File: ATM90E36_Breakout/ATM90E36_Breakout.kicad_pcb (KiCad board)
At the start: 2 copper layers, 50 x 50 mm, 75 parts, among them IC1 ATM90E36, Q1 FA-128

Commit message: Fix references and SCH/PCB linkage
Signed-off-by: Tisham Dhar <whatnickd@gmail.com>
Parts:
- renumbered CTA to CTA1, CTB to CTB1, CTC to CTC1, CTN to CTN1, DMA to DMA1, UAUB to UAUB1, UCUN to UCUN1
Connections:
- net CF1 renamed /CF1
- net CF2 renamed /CF2
- net CF3 renamed /CF3
- net CF4 renamed /CF4
- net DMA renamed /DMA
- net IA+ renamed /IA+
- net IA- renamed /IA-
- net IAN renamed /IAN
- net IAP renamed /IAP
- net IB+ renamed /IB+
- net IB- renamed /IB-
- net IBN renamed /IBN
- net IBP renamed /IBP
- net IC+ renamed /IC+
- net IC- renamed /IC-
- net ICN renamed /ICN
- net ICP renamed /ICP
- net IN+ renamed /IN+
- net IN- renamed /IN-
- net INN renamed /INN
- net INP renamed /INP
- net IRQ1 renamed /IRQ1
- net IRQ2 renamed /IRQ2
- net MISO renamed /MISO
- net MOSI renamed /MOSI
- net PM0 renamed /PM0
- net PM1 renamed /PM1
- net SCLK renamed /SCLK
- net UA renamed /UA
- net UB renamed /UB
- net UC renamed /UC
- net VAP renamed /VAP
- net VBP renamed /VBP
- net VCP renamed /VCP
- net WARN renamed /WARN
- net ZX0 renamed Net-(IC1-Pad22)
- net ZX1 renamed Net-(IC1-Pad23)
- net ZX2 renamed Net-(IC1-Pad24)
- net ~CS renamed /~CS
- CTA1 pad COM2: (no net) -> Net-(CTA1-PadCOM2)
- CTA1 pad LS: (no net) -> Net-(CTA1-PadLS)
- CTA1 pad R: (no net) -> Net-(CTA1-PadR)
- CTA1 pad RS: (no net) -> Net-(CTA1-PadRS)
- CTB1 pad COM2: (no net) -> Net-(CTB1-PadCOM2)
- CTB1 pad LS: (no net) -> Net-(CTB1-PadLS)
- CTB1 pad R: (no net) -> Net-(CTB1-PadR)
- CTB1 pad RS: (no net) -> Net-(CTB1-PadRS)
- CTC1 pad COM2: (no net) -> Net-(CTC1-PadCOM2)
- CTC1 pad LS: (no net) -> Net-(CTC1-PadLS)
- CTC1 pad R: (no net) -> Net-(CTC1-PadR)
- CTC1 pad RS: (no net) -> Net-(CTC1-PadRS)
- CTN1 pad COM2: (no net) -> Net-(CTN1-PadCOM2)
- CTN1 pad LS: (no net) -> Net-(CTN1-PadLS)
- CTN1 pad R: (no net) -> Net-(CTN1-PadR)
- CTN1 pad RS: (no net) -> Net-(CTN1-PadRS)
- IC1 pad 35: (no net) -> Net-(IC1-Pad35)
- IC1 pad 45: (no net) -> Net-(IC1-Pad45)
- IC1 pad 46: (no net) -> Net-(IC1-Pad46)

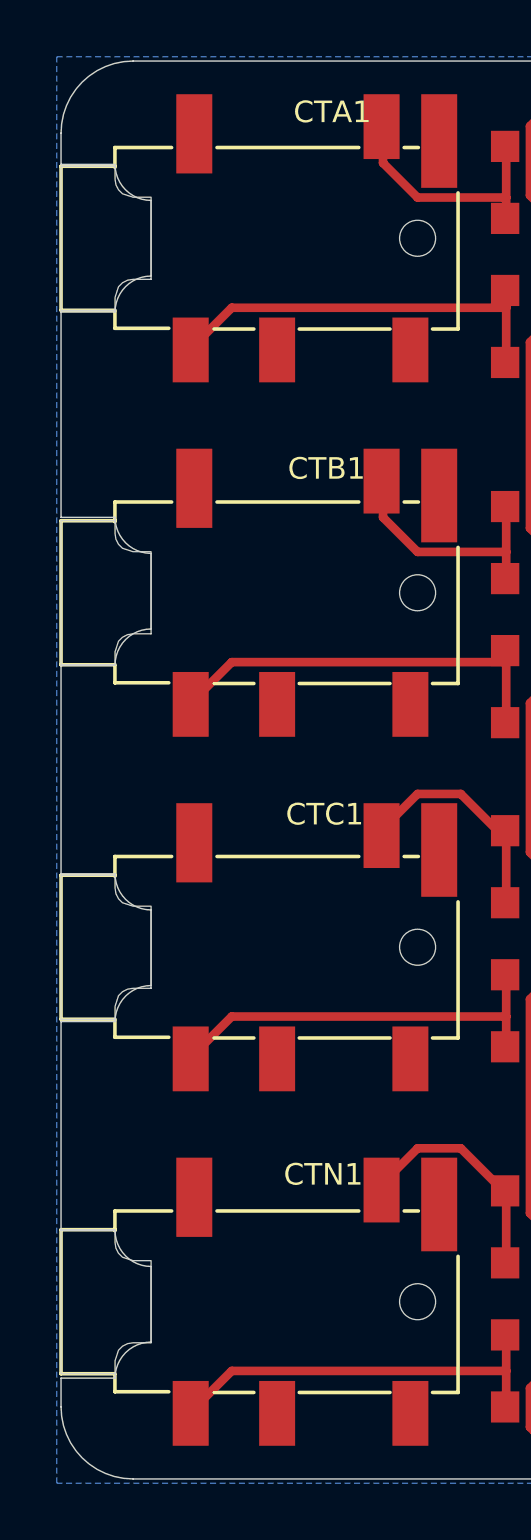
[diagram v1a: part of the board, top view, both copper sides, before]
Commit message: Remove edge cuts from parts to fix board outline
Signed-off-by: Tisham Dhar <whatnickd@gmail.com>
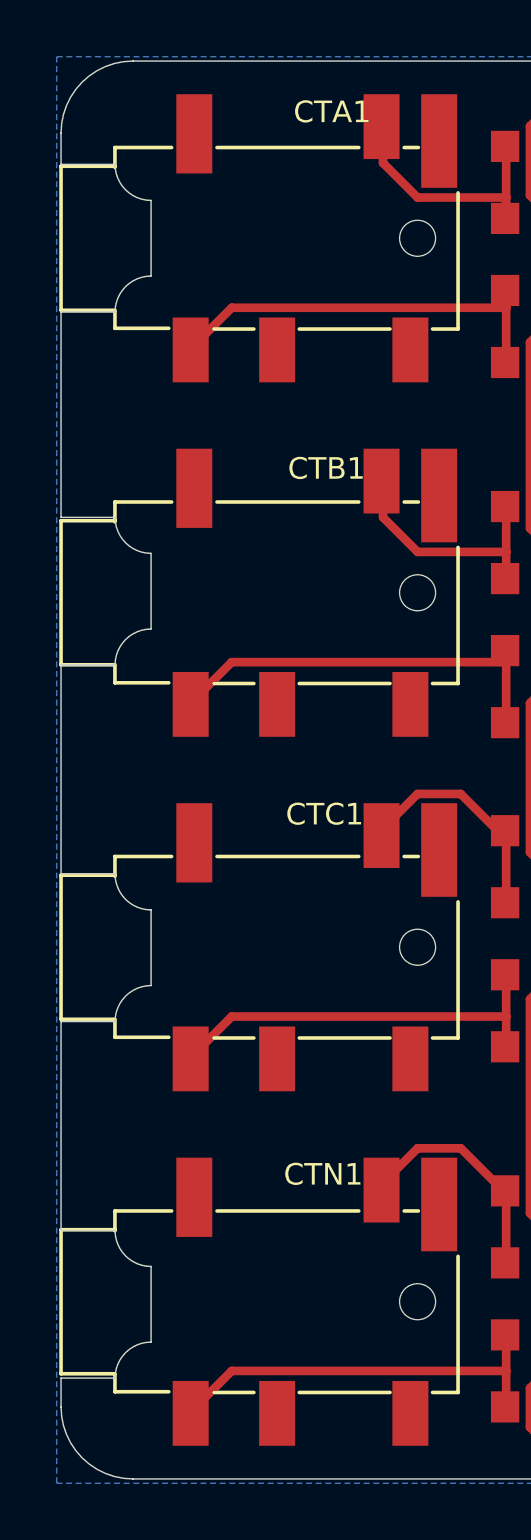
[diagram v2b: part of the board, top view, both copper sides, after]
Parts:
- CTA1, CTB1, CTC1, CTN1: footprint AUDIO6P-SMD-3.5-14.0X6.4X5.0MM -> ATM90E36_Breakout:AUDIO6P-SMD-3.5-14.0X6.4X5.0MM

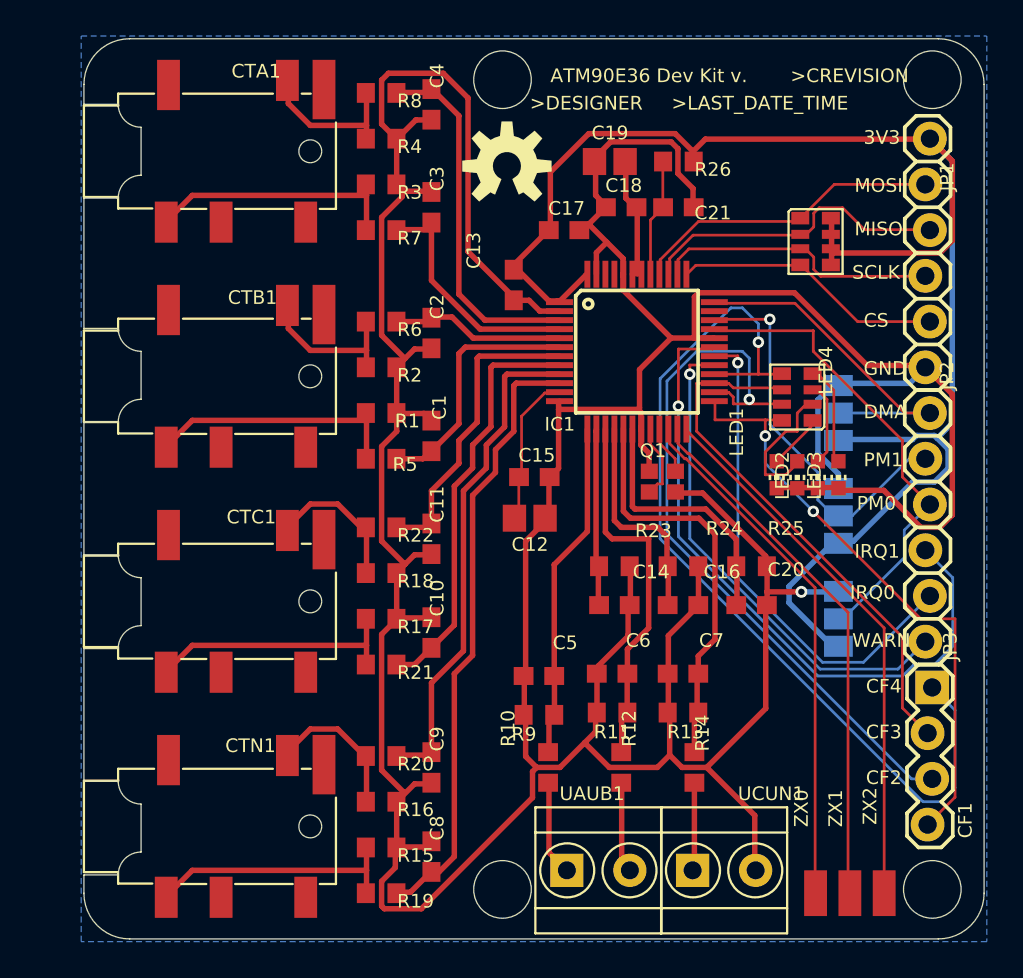
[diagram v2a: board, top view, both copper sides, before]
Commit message: Fix up silk screens
Signed-off-by: Tisham Dhar <whatnickd@gmail.com>
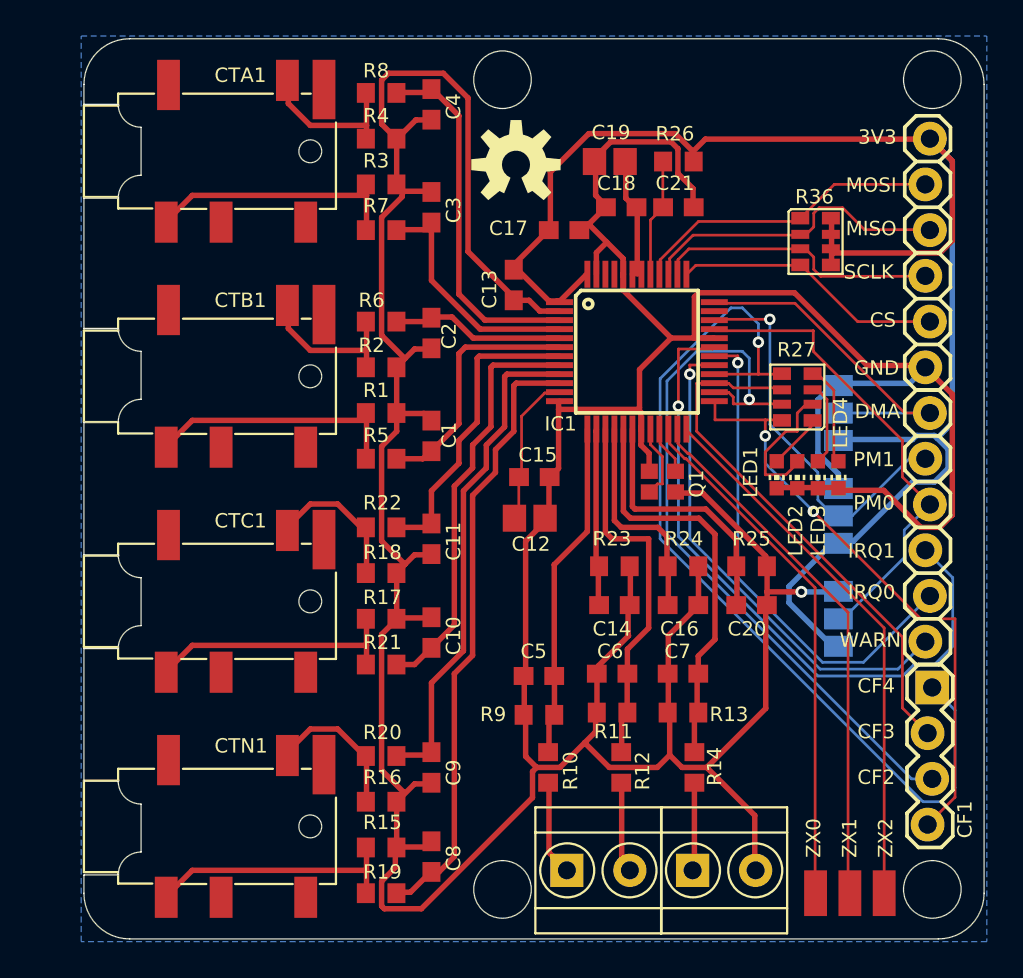
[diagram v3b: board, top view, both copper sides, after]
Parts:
- LOGO1: value OSHW-LOGOM -> Logo_Open_Hardware_Small; footprint OSHW-LOGO-M -> ATM90E36_Breakout:OSHW-LOGO-M
- moved LOGO1 0.51 mm to (147.5, 87.0)
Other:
- board text added: "ATM90E3x Breakout v0.2 Tisham (whatnick) Dhar 2019-12-26 OSHW TAPR"
- board text removed: ">CREVISION"
- board text removed: ">DESIGNER"
- board text removed: ">LAST_DATE_TIME"
- board text removed: "ATM90E36 Dev Kit v."

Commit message: Add full BOM and Gerbers
Signed-off-by: Tisham Dhar <whatnickd@gmail.com>
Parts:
- removed @HOLE0, @HOLE1, @HOLE2, @HOLE3: , 
- added Hole0: MountingHole, , F.Cu at (146.8, 82.3)
- added Hole1: MountingHole, , F.Cu at (170.6, 82.3)
- added Hole2: MountingHole, , F.Cu at (170.6, 127.3)
- added Hole3: MountingHole, , F.Cu at (146.8, 127.3)
- LED2: value GRN -> RED
- LED3: value BLU -> RED
- LED4: value YEL -> RED
- ZX0, ZX2: value ZX0 -> ZX
- ZX1: value ZX1 -> ZX
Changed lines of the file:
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@@
     (pcbplotparams
       (layerselection 0x010fc_ffffffff)
-      (usegerberextensions false)
+      (usegerberextensions true)
       (usegerberattributes false)
       (usegerberadvancedattributes false)
@@
       (outputformat 1)
       (mirror false)
-      (drillshape 1)
+      (drillshape 0)
       (scaleselection 1)
-      (outputdirectory ""))
+      (outputdirectory "gerbers"))
   )
   (net 0 "")
@@
   (module "" (layer Top)
     (at 146.7511 82.2786)
-    (fp_text reference @HOLE0 (at 0 0) (layer F.SilkS) hide
+    (fp_text reference Hole0 (at 0 0) (layer F.SilkS) hide
       (effects (font (size 0.8 0.8) (thickness 0.2)))
     )
-    (fp_text value "" (at 0 0) (layer F.SilkS)
+    (fp_text value MountingHole (at 0 0) (layer F.SilkS) hide
       (effects (font (size 1.27 1.27) (thickness 0.15)))
     )
@@
   (module "" (layer Top)
     (at 170.6261 82.2786)
-    (fp_text reference @HOLE1 (at 0 0) (layer F.SilkS) hide
+    (fp_text reference Hole1 (at 0 0) (layer F.SilkS) hide
       (effects (font (size 0.8 0.8) (thickness 0.2)))
     )
-    (fp_text value "" (at 0 0) (layer F.SilkS)
+    (fp_text value MountingHole (at 0 0) (layer F.SilkS) hide
       (effects (font (size 1.27 1.27) (thickness 0.15)))
     )
@@
   (module "" (layer Top)
     (at 170.6261 127.2536)
-    (fp_text reference @HOLE2 (at 0 0) (layer F.SilkS) hide
+    (fp_text reference Hole2 (at 0 0) (layer F.SilkS) hide
       (effects (font (size 0.8 0.8) (thickness 0.2)))
     )
-    (fp_text value "" (at 0 0) (layer F.SilkS)
+    (fp_text value MountingHole (at 0 0) (layer F.SilkS) hide
       (effects (font (size 1.27 1.27) (thickness 0.15)))
     )
@@
   (module "" (layer Top)
     (at 146.7511 127.2536)
-    (fp_text reference @HOLE3 (at 0 0) (layer F.SilkS) hide
+    (fp_text reference Hole3 (at 0 0) (layer F.SilkS) hide
       (effects (font (size 0.8 0.8) (thickness 0.2)))
     )
-    (fp_text value "" (at 0 0) (layer F.SilkS)
+    (fp_text value MountingHole (at 0 0) (layer F.SilkS) hide
       (effects (font (size 1.27 1.27) (thickness 0.15)))
     )
@@
       (effects (font (size 0.8 0.8) (thickness 0.2)) (justify left bottom))
     )
-    (fp_text value ZX0 (at 0 0) (layer F.Fab)
+    (fp_text value ZX (at 0 0) (layer F.Fab)
       (effects (font (size 0.76 0.76) (thickness 0.0608)) (justify left bottom))
     )
@@
       (effects (font (size 0.8 0.8) (thickness 0.2)) (justify left bottom))
     )
-    (fp_text value ZX1 (at 0 0) (layer F.Fab)
+    (fp_text value ZX (at 0 0) (layer F.Fab)
       (effects (font (size 0.76 0.76) (thickness 0.0608)) (justify left bottom))
     )
@@
       (effects (font (size 0.8 0.8) (thickness 0.2)) (justify left bottom))
     )
-    (fp_text value ZX0 (at 0 0) (layer F.Fab)
+    (fp_text value ZX (at 0 0) (layer F.Fab)
       (effects (font (size 0.76 0.76) (thickness 0.0608)) (justify left bottom))
     )
@@
       (effects (font (size 0.8 0.8) (thickness 0.2)) (justify left bottom))
     )
-    (fp_text value GRN (at 1.905 0.635 90) (layer F.Fab)
+    (fp_text value RED (at 1.905 0.635 90) (layer F.Fab)
       (effects (font (size 0.76 0.76) (thickness 0.0608)) (justify left bottom))
     )
@@
       (effects (font (size 0.8 0.8) (thickness 0.2)) (justify left bottom))
     )
-    (fp_text value BLU (at 1.905 0.635 90) (layer F.Fab)
+    (fp_text value RED (at 1.905 0.635 90) (layer F.Fab)
       (effects (font (size 0.76 0.76) (thickness 0.0608)) (justify left bottom))
     )
@@
       (effects (font (size 0.8 0.8) (thickness 0.2)) (justify left bottom))
     )
-    (fp_text value YEL (at 1.905 0.635 90) (layer F.Fab)
-      (effects (font (size 0.76 0.76) (thickness 0.0608)) (justify left bottom))
-    )
+    (fp_text value RED (at 1.905 0.635 90) (layer F.Fab)
+      (effects (font (size 0.76 0.76) (thickness 0.0608)) (justify left bottom))
+    )

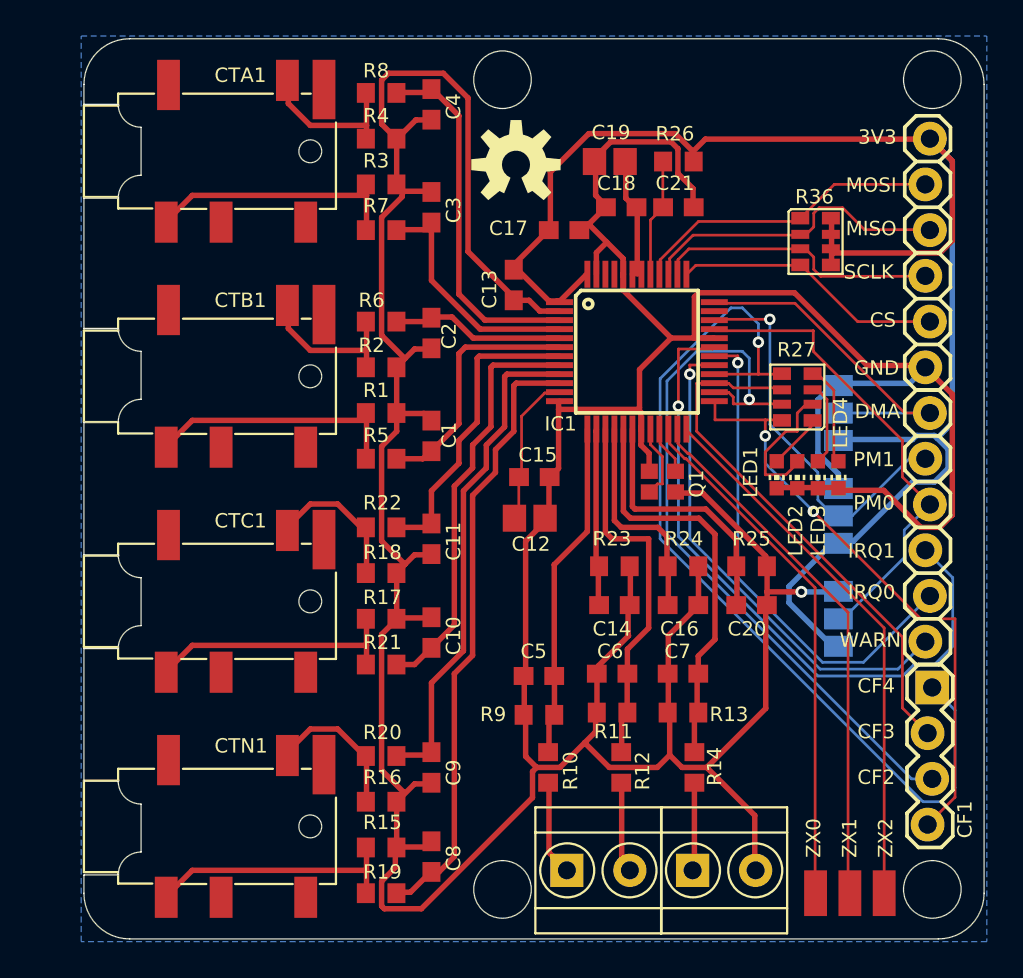
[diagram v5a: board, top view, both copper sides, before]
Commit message: Updated Stereojacks to mainstream ones
Signed-off-by: Tisham Dhar <whatnickd@gmail.com>
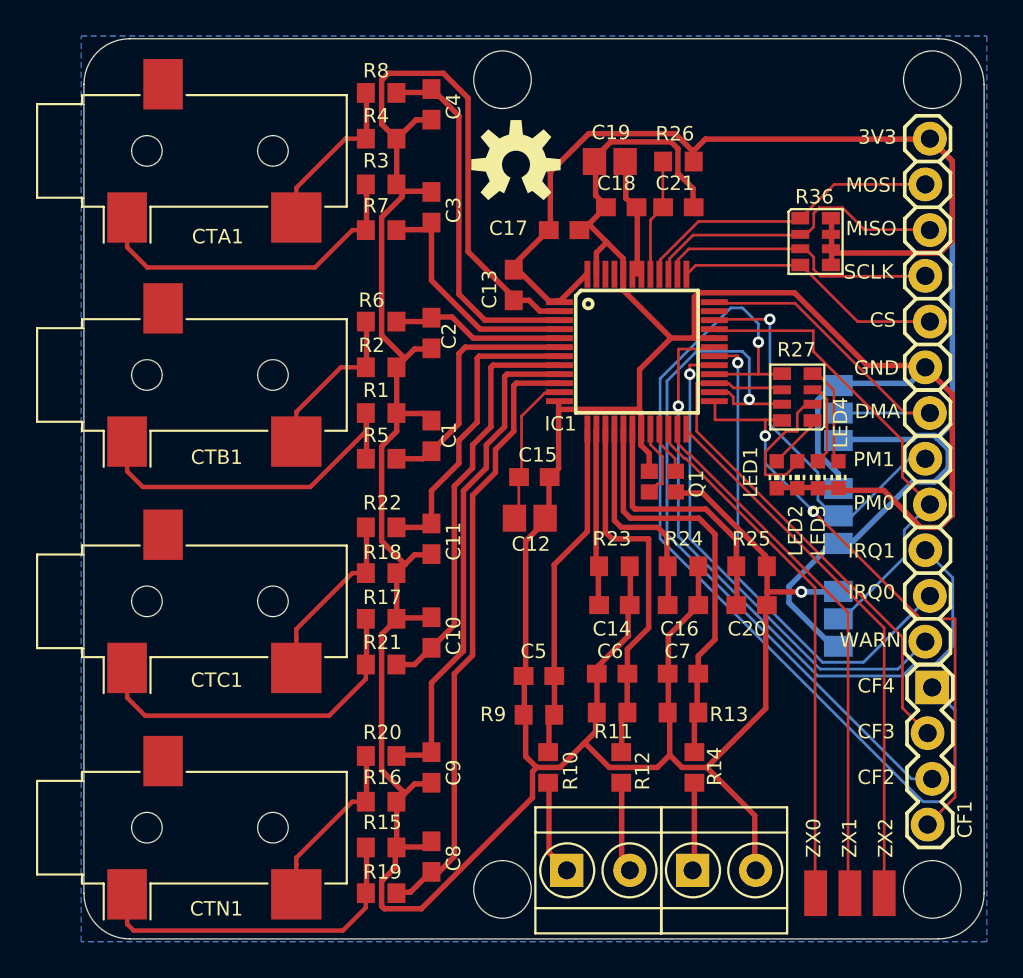
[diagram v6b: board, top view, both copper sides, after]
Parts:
- CTA1, CTB1, CTC1, CTN1: value ST-PJ-312 -> AudioJack3; footprint ATM90E36_Breakout:AUDIO6P-SMD-3.5-14.0X6.4X5.0MM -> Connector_Audio:Jack_3.5mm_CUI_SJ-3523-SMT_Horizontal
- moved CTB1 6.00 mm to (129.5, 98.7), turned to 90 degrees
- moved CTN1 6.00 mm to (129.5, 123.8), turned to 90 degrees
- moved CTA1 6.00 mm to (129.5, 86.2), turned to 90 degrees
- moved CTC1 6.00 mm to (129.5, 111.3), turned to 90 degrees
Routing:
- net /IB-: track 14.7 -> 20.6 mm
- net /IC-: track 14.4 -> 19.6 mm
- net /IN-: track 14.3 -> 19.0 mm
- net /IA-: track 14.4 -> 18.8 mm
- net /IC+: track 8.22 -> 10.3 mm
- net /IN+: track 8.30 -> 9.90 mm
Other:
- outline, holes or cut-outs redrawn

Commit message: Upgrade to KiCAD 7 and order from Elecrow
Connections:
- net /~CS renamed /~{CS}
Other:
- net class Default removed

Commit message: Update silkscreen to avoid wiring confusion
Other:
- board text added: "ATM90E3x Breakout v0.3 Tisham (whatnick) Dhar 2025-03-22 OSHW TAPR"
- board text added: "UA"
- board text added: "UB"
- board text added: "UC"
- board text added: "UN"
- board text removed: "ATM90E3x Breakout v0.2 Tisham (whatnick) Dhar 2019-12-26 OSHW TAPR"
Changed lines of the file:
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@@
     (at 152.0761 126.1936)
     (attr through_hole)
-    (fp_text reference "UAUB1" (at -2.159 -3.81) (layer "B.SilkS")
+    (fp_text reference "UAUB1" (at -2.159 -3.81) (layer "B.SilkS") hide
         (effects (font (size 0.8 0.8) (thickness 0.2)) (justify right bottom mirror))
     )
@@
     (at 159.0611 126.1936)
     (attr through_hole)
-    (fp_text reference "UCUN1" (at -2.3111 -3.6936) (layer "B.SilkS")
+    (fp_text reference "UCUN1" (at -2.3111 -3.6936) (layer "B.SilkS") hide
         (effects (font (size 0.8 0.8) (thickness 0.2)) (justify right bottom mirror))
     )
@@
   (gr_line (start 123.5011 126.4476) (end 123.5011 127.4636)
     (stroke (width 0.05) (type solid)) (layer "Edge.Cuts"))
-  (gr_text "ATM90E3x Breakout v0.2\nTisham (whatnick) Dhar\n2019-12-26\nOSHW TAPR" (at 147 94.5) (layer "B.SilkS")
+  (gr_text "ATM90E3x Breakout v0.3\nTisham (whatnick) Dhar\n2025-03-22\nOSHW TAPR" (at 147 94.5) (layer "B.SilkS")
     (effects (font (size 0.8 0.8) (thickness 0.2)) (justify mirror))
   )
@@
     (effects (font (size 0.8 0.8) (thickness 0.2)) (justify left bottom mirror))
   )
+  (gr_text "UN" (at 162.56 122.428) (layer "B.SilkS")
+    (effects (font (size 1.5 1.5) (thickness 0.3) bold) (justify left bottom mirror))
+  )
   (gr_text "IRQ1" (at 169.0941 108.7946) (layer "B.SilkS")
     (effects (font (size 0.8 0.8) (thickness 0.2)) (justify left bottom mirror))
   )
+  (gr_text "UC" (at 159.004 122.428) (layer "B.SilkS")
+    (effects (font (size 1.5 1.5) (thickness 0.3) bold) (justify left bottom mirror))
+  )
+  (gr_text "UB" (at 155.448 122.428) (layer "B.SilkS")
+    (effects (font (size 1.5 1.5) (thickness 0.3) bold) (justify left bottom mirror))
+  )
   (gr_text "CF3" (at 168.7131 118.9546) (layer "B.SilkS")
     (effects (font (size 0.8 0.8) (thickness 0.2)) (justify left bottom mirror))
@@
     (effects (font (size 0.8 0.8) (thickness 0.2)) (justify left bottom mirror))
   )
+  (gr_text "UA" (at 151.892 122.428) (layer "B.SilkS")
+    (effects (font (size 1.5 1.5) (thickness 0.3) bold) (justify left bottom mirror))
+  )
   (gr_text "MOSI" (at 168.8401 88.6016) (layer "B.SilkS")
